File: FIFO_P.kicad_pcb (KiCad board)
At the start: 4 copper layers, 100 x 100 mm, 76 parts, among them J1 Vin +, J2 Vin -, J3 ICLK, J4 Vout, J5 Jack-DC, SW1 Rotary_Encoder_61C, U1 SN74LVC2G157_MUX_TI, U10 AD7840, U11 LM2940CT-5.0, U12 UA79M05CKCS_-5V, U13 LM2940CT-3.3, U2 IDT_ICS551, U3 LTC1740, U4 ARDUINO_DUE_FIFO_P_COMMANDS, U5 IDT_72V2105, U6 TXB0104, U7 TXB0104, U8 TXB0104, U9 TXB0104

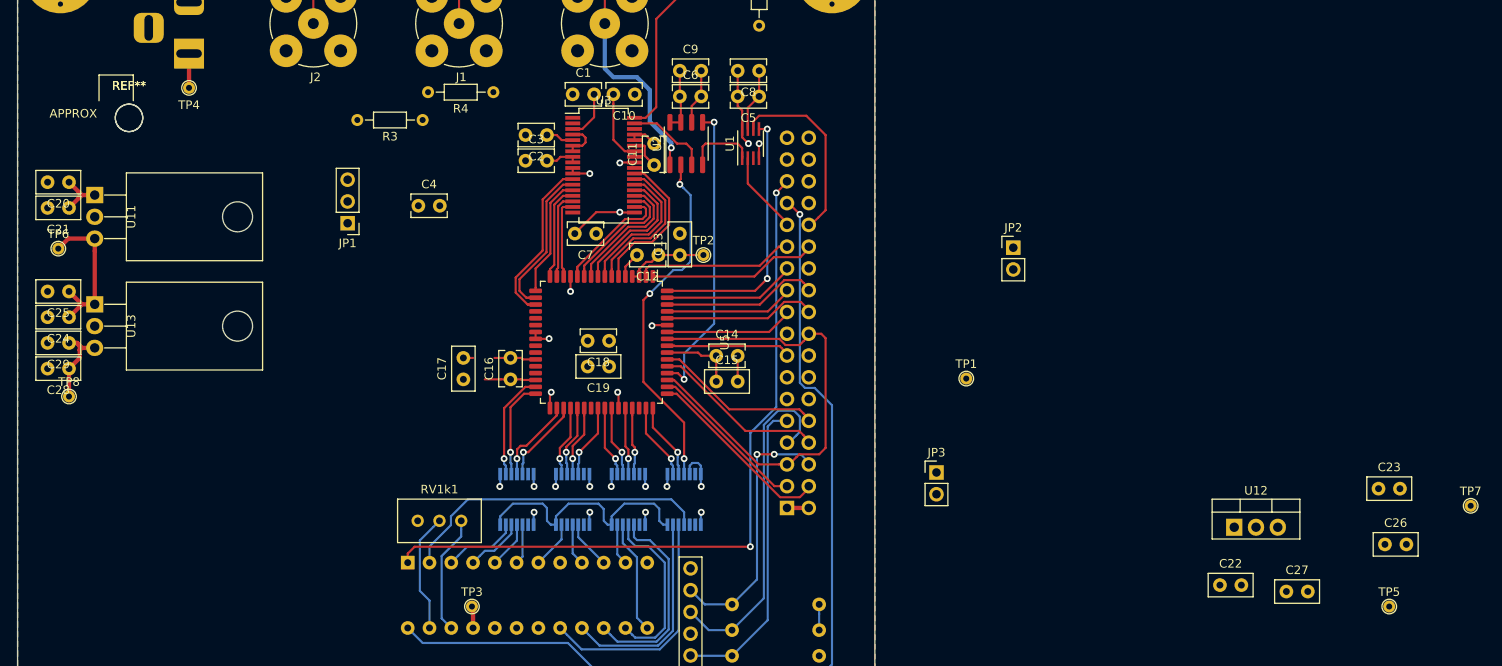
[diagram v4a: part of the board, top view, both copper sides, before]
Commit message: Added inverter for -5V
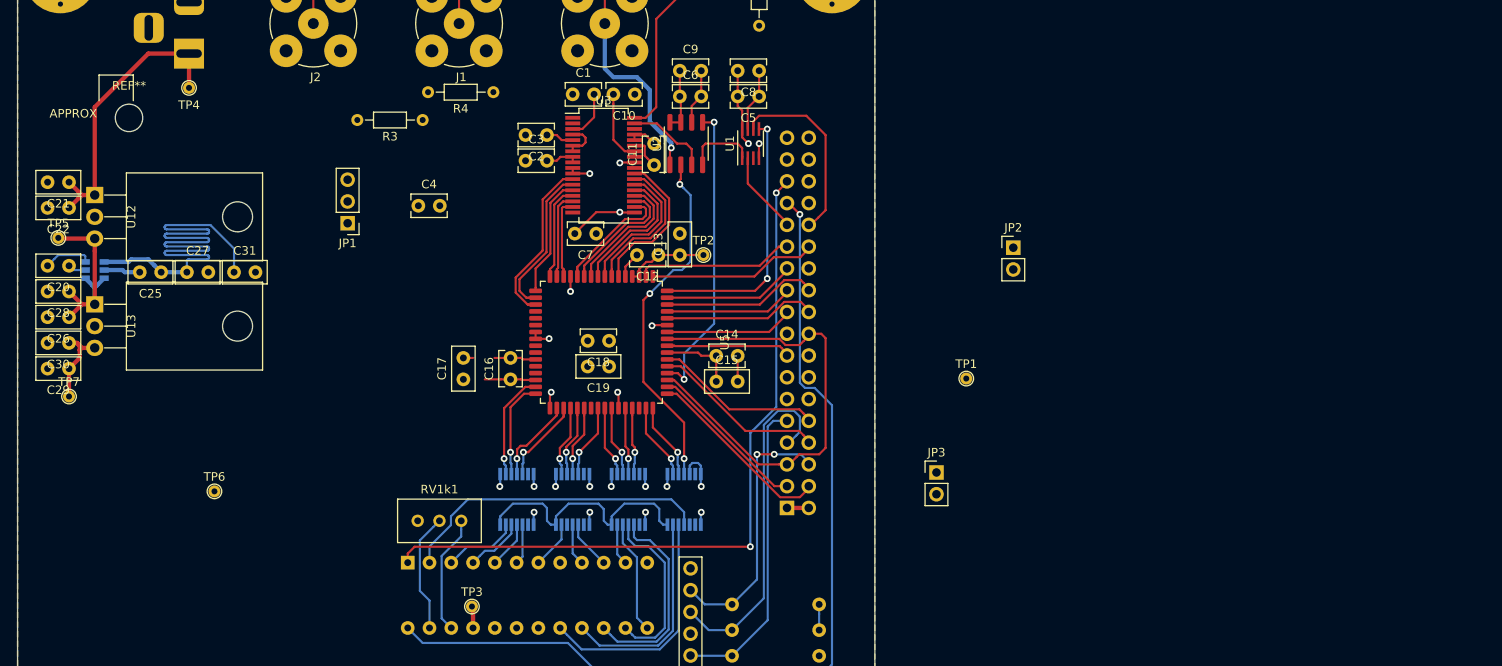
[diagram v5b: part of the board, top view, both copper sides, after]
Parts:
- removed the C22 at (189.8, 125.5)
- removed C23: .47uF, Capacitor_THT:C_Disc_D5.0mm_W2.5mm_P2.50mm
- removed the C26 at (209.0, 120.8)
- removed the REF** at (62.5, 71.0)
- removed the TP5 at (209.5, 128.0)
- removed the TP7 at (219.0, 116.2)
- removed the U12 at (191.4, 118.8)
- added C20: .47uF, Capacitor_THT:C_Disc_D5.0mm_W2.5mm_P2.50mm, F.Cu at (55.5, 88.2)
- added C25: .47uF, Capacitor_THT:C_Disc_D5.0mm_W2.5mm_P2.50mm, F.Cu at (66.2, 89.0)
- added C31: 22uF, Capacitor_THT:C_Disc_D5.0mm_W2.5mm_P2.50mm, F.Cu at (74.8, 89.0)
- added TP6: TestPoint, FIFO_P:Test_Pin, F.Cu at (72.5, 114.6)
- added U11: LM2776, Package_TO_SOT_SMD:SOT-23-6, B.Cu at (58.5, 88.8)
- C27: value .47uF -> 22uF
- moved C27 133.6 mm to (69.2, 89.0)
- moved TP5 1.25 mm to (54.2, 85.0)
- renumbered C20 to C21, C21 to C22, C24 to C26, C25 to C28, C28 to C29, C29 to C30, TP6 to TP5, TP8 to TP7, U11 to U12
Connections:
- C12 pad 2: GND -> +5V
- C13 pad 2: GND -> +5V
- C14 pad 2: GND -> +5V
- C15 pad 2: GND -> +5V
- C16 pad 2: GND -> +5V
- C17 pad 2: GND -> +5V
- C18 pad 1: GND -> +5V
- C19 pad 1: GND -> +5V
- C21 pad 2: GND -> +5V
- C22 pad 2: GND -> +5V
- C26 pad 2: GND -> +5V
- C27 pad 2: Net-(C22-Pad2) -> +5V
- C28 pad 2: GND -> +5V
- C29 pad 2: GND -> +5V
- C30 pad 2: GND -> +5V
- C5 pad 1: GND -> +5V
- C6 pad 2: GND -> +5V
- C7 pad 1: GND -> +5V
- C8 pad 1: GND -> +5V
- C9 pad 2: GND -> +5V
- J3 pad 2: GND -> +5V
- J5 pad 2: GND -> +5V
- JP2 pad 1: GND -> +5V
- JP3 pad 1: GND -> +5V
- R5 pad 2: GND -> +5V
- R6 pad 2: GND -> +5V
- R8 pad 1: GND -> +5V
- RV1k1 pad 3: GND -> +5V
- SW1 pad 1: GND -> +5V
- U1 pad 4: GND -> +5V
- U1 pad 7: GND -> +5V
- U10 pad 12: GND -> +5V
- U12 pad 2: GND -> +5V
- U13 pad 2: GND -> +5V
- U2 pad 6: GND -> +5V
- U3 pad 10: GND -> +5V
- U3 pad 11: GND -> +5V
- U3 pad 28: GND -> +5V
- U4 pad GND: GND -> +5V
- U5 pad 13: GND -> +5V
- U5 pad 23: GND -> +5V
- U5 pad 24: GND -> +5V
- U5 pad 27: GND -> +5V
- U5 pad 33: GND -> +5V
- U5 pad 39: GND -> +5V
- U5 pad 46: GND -> +5V
- U5 pad 5: GND -> +5V
- U5 pad 59: GND -> +5V
- U6 pad 7: GND -> +5V
- U7 pad 7: GND -> +5V
- U8 pad 7: GND -> +5V
- U9 pad 5: GND -> +5V
- U9 pad 7: GND -> +5V
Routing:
- net -5V: track 11.5 -> 76.4 mm
- net +5V: track 58.5 -> 117.3 mm, vias 0 -> 11
- net GND: track 49.5 -> 0.00 mm, vias 11 -> 0
- net Net-(C21-Pad1): track 10.5 -> 34.3 mm
- net Net-(C20-Pad2): track 0.00 -> 5.64 mm
- net Net-(C20-Pad1): track 0.00 -> 2.11 mm
- added copper zone on B.Cu, net +5V
- added copper zone on In1.Cu, net +5V
- removed copper zone on B.Cu, net -5V
- removed copper zone on In1.Cu, net GND

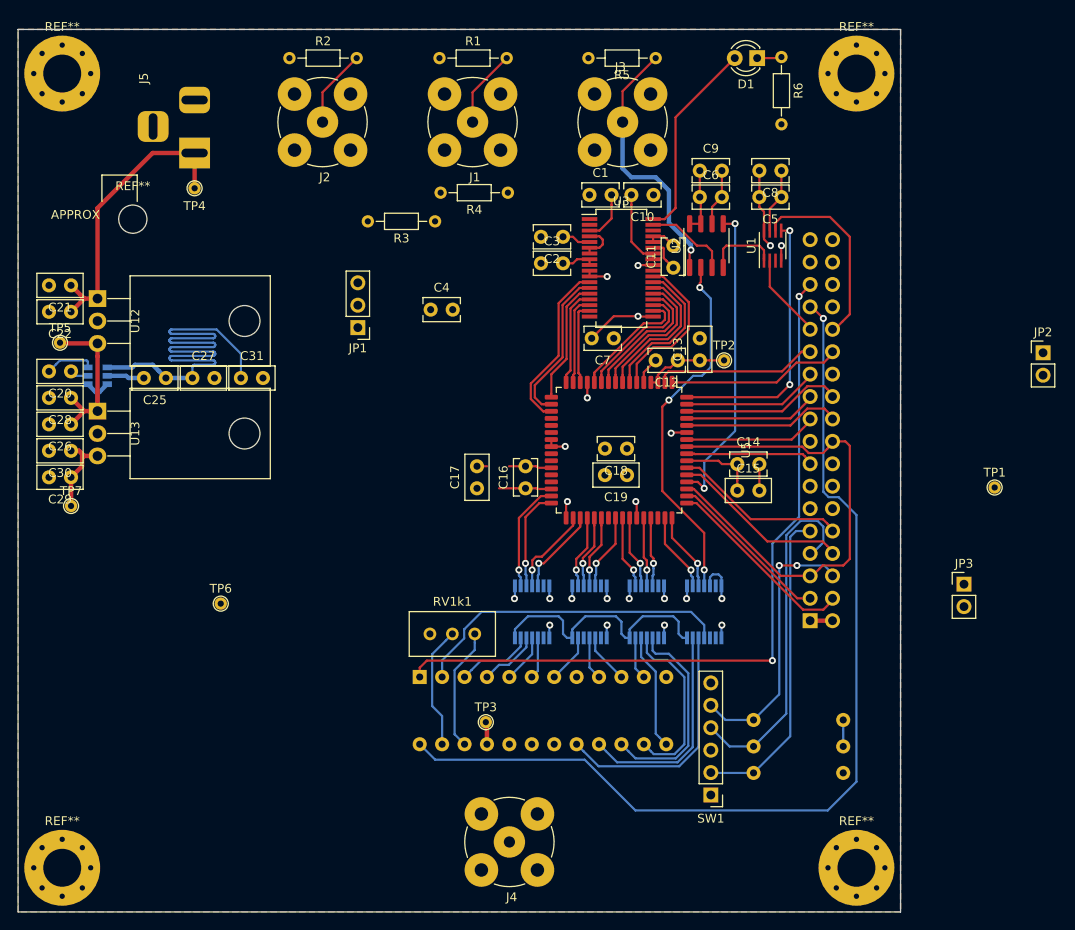
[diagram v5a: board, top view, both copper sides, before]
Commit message: Partial jumpers
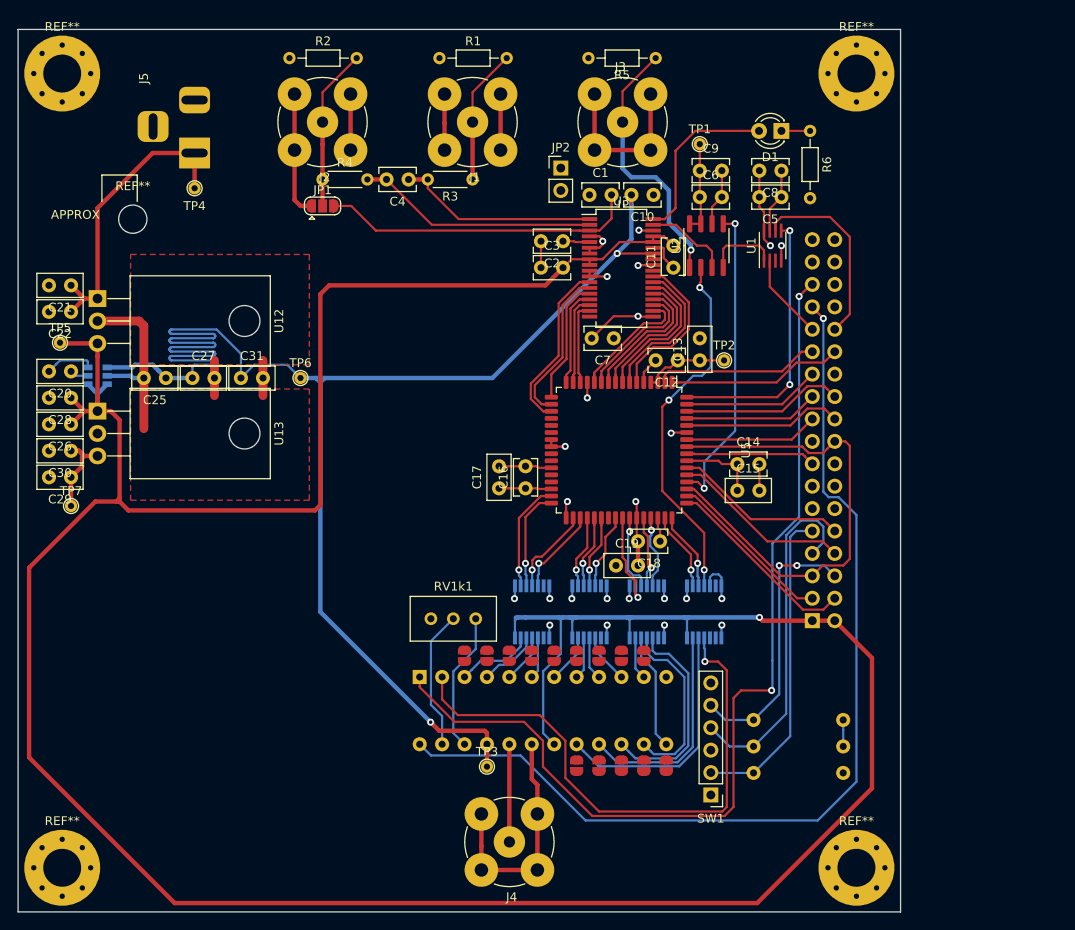
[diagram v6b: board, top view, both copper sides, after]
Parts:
- removed JP3: Jumper, Connector_PinHeader_2.54mm:PinHeader_1x02_P2.54mm_Vertical
- added REF**: SolderJumper-2_P1.3mm_Open_RoundedPad1.0x1.5mm, Jumper:SolderJumper-2_P1.3mm_Open_RoundedPad1.0x1.5mm, F.Cu at (112.8, 132.9)
- added REF**: SolderJumper-2_P1.3mm_Open_RoundedPad1.0x1.5mm, Jumper:SolderJumper-2_P1.3mm_Open_RoundedPad1.0x1.5mm, F.Cu at (110.2, 120.5)
- added REF**: SolderJumper-2_P1.3mm_Open_RoundedPad1.0x1.5mm, Jumper:SolderJumper-2_P1.3mm_Open_RoundedPad1.0x1.5mm, F.Cu at (107.7, 120.5)
- added REF**: SolderJumper-2_P1.3mm_Open_RoundedPad1.0x1.5mm, Jumper:SolderJumper-2_P1.3mm_Open_RoundedPad1.0x1.5mm, F.Cu at (105.2, 120.5)
- added REF**: SolderJumper-2_P1.3mm_Open_RoundedPad1.0x1.5mm, Jumper:SolderJumper-2_P1.3mm_Open_RoundedPad1.0x1.5mm, F.Cu at (102.6, 120.5)
- added REF**: SolderJumper-2_P1.3mm_Open_RoundedPad1.0x1.5mm, Jumper:SolderJumper-2_P1.3mm_Open_RoundedPad1.0x1.5mm, F.Cu at (100.1, 120.5)
- added REF**: SolderJumper-2_P1.3mm_Open_RoundedPad1.0x1.5mm, Jumper:SolderJumper-2_P1.3mm_Open_RoundedPad1.0x1.5mm, F.Cu at (115.3, 132.9)
- added REF**: SolderJumper-2_P1.3mm_Open_RoundedPad1.0x1.5mm, Jumper:SolderJumper-2_P1.3mm_Open_RoundedPad1.0x1.5mm, F.Cu at (117.9, 132.9)
- added REF**: SolderJumper-2_P1.3mm_Open_RoundedPad1.0x1.5mm, Jumper:SolderJumper-2_P1.3mm_Open_RoundedPad1.0x1.5mm, F.Cu at (120.4, 132.9)
- added REF**: SolderJumper-2_P1.3mm_Open_RoundedPad1.0x1.5mm, Jumper:SolderJumper-2_P1.3mm_Open_RoundedPad1.0x1.5mm, F.Cu at (123.0, 132.9)
- added REF**: SolderJumper-2_P1.3mm_Open_RoundedPad1.0x1.5mm, Jumper:SolderJumper-2_P1.3mm_Open_RoundedPad1.0x1.5mm, F.Cu at (120.4, 120.5)
- added REF**: SolderJumper-2_P1.3mm_Open_RoundedPad1.0x1.5mm, Jumper:SolderJumper-2_P1.3mm_Open_RoundedPad1.0x1.5mm, F.Cu at (117.9, 120.5)
- added REF**: SolderJumper-2_P1.3mm_Open_RoundedPad1.0x1.5mm, Jumper:SolderJumper-2_P1.3mm_Open_RoundedPad1.0x1.5mm, F.Cu at (115.3, 120.5)
- added REF**: SolderJumper-2_P1.3mm_Open_RoundedPad1.0x1.5mm, Jumper:SolderJumper-2_P1.3mm_Open_RoundedPad1.0x1.5mm, F.Cu at (112.8, 120.5)
- JP1: footprint Connector_PinHeader_2.54mm:PinHeader_1x03_P2.54mm_Vertical -> Jumper:SolderJumper-3_P1.3mm_Open_RoundedPad1.0x1.5mm
- R3, R4: footprint Resistor_THT:R_Axial_DIN0204_L3.6mm_D1.6mm_P7.62mm_Horizontal -> Resistor_THT:R_Axial_DIN0204_L3.6mm_D1.6mm_P5.08mm_Horizontal
- moved JP2 58.5 mm to (111.0, 65.2)
- moved TP1 51.3 mm to (126.8, 62.5)
- moved TP6 27.1 mm to (81.5, 89.0)
- moved R4 21.1 mm to (84.0, 66.5), turned to 0 degrees
- moved C4 15.0 mm to (93.8, 66.5), turned to 180 degrees
- moved JP1 14.4 mm to (84.0, 69.5), turned to 0 degrees
- moved C18 11.1 mm to (122.2, 107.5)
- moved C19 10.3 mm to (117.2, 110.2), turned to 0 degrees
- moved R6 8.98 mm to (139.2, 61.0)
- moved D1 8.70 mm to (136.0, 61.0)
- moved R3 6.37 mm to (101.0, 66.5)
- moved TP3 5.04 mm to (102.6, 133.0)
- moved C17 2.50 mm to (104.0, 101.5)
- moved RV1k1 1.73 mm to (101.4, 116.3)
- moved C2 0.50 mm to (111.2, 73.5)
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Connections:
- C12 pad 2: +5V -> GND
- C13 pad 2: +5V -> GND
- C14 pad 2: +5V -> GND
- C15 pad 2: +5V -> GND
- C16 pad 2: +5V -> GND
- C17 pad 2: +5V -> GND
- C18 pad 1: +5V -> GND
- C19 pad 1: +5V -> GND
- C21 pad 2: +5V -> GND
- C22 pad 2: +5V -> GND
- C25 pad 2: +5V -> GND
- C26 pad 2: +5V -> GND
- C27 pad 2: +5V -> GND
- C28 pad 2: +5V -> GND
- C29 pad 2: +5V -> GND
- C30 pad 2: +5V -> GND
- C31 pad 2: +5V -> GND
- C5 pad 1: +5V -> GND
- C6 pad 2: +5V -> GND
- C7 pad 1: +5V -> GND
- C8 pad 1: +5V -> GND
- C9 pad 2: +5V -> GND
- J3 pad 2: +5V -> GND
- J5 pad 2: +5V -> GND
- JP2 pad 1: +5V -> GND
- R5 pad 2: +5V -> GND
- R6 pad 2: +5V -> GND
- R8 pad 1: +5V -> GND
- RV1k1 pad 3: +5V -> GND
- SW1 pad 1: +5V -> GND
- U1 pad 4: +5V -> GND
- U1 pad 7: +5V -> GND
- U10 pad 12: +5V -> GND
- U11 pad 2: +5V -> GND
- U12 pad 2: +5V -> GND
- U13 pad 2: +5V -> GND
- U2 pad 6: +5V -> GND
- U3 pad 10: +5V -> GND
- U3 pad 11: +5V -> GND
- U3 pad 28: +5V -> GND
- U4 pad GND: +5V -> GND
- U5 pad 13: +5V -> GND
- U5 pad 23: +5V -> GND
- U5 pad 24: +5V -> GND
- U5 pad 27: +5V -> GND
- U5 pad 33: +5V -> GND
- U5 pad 39: +5V -> GND
- U5 pad 46: +5V -> GND
- U5 pad 5: +5V -> GND
- U5 pad 59: +5V -> GND
- U6 pad 7: +5V -> GND
- U7 pad 7: +5V -> GND
- U8 pad 7: +5V -> GND
- U9 pad 5: +5V -> GND
- U9 pad 7: +5V -> GND
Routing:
- net +5V: track 117.3 -> 356.2 mm, vias 11 -> 1
- net -5V: track 76.4 -> 183.6 mm, vias 0 -> 2
- net GND: track 0.00 -> 100.7 mm, vias 0 -> 11
- net GNDA: track 8.37 -> 46.2 mm, vias 0 -> 2
- net Net-(C1-Pad2): track 5.73 -> 35.8 mm
- net Net-(C4-Pad2): track 0.00 -> 27.3 mm
- net LDAC5V: track 36.5 -> 63.8 mm, vias 0 -> 1
- net Net-(J4-Pad2): track 0.00 -> 27.2 mm
- net Net-(U10-Pad1): track 85.9 -> 109.9 mm
- net Net-(C4-Pad1): track 0.00 -> 22.9 mm
- net Net-(J4-Pad1): track 0.00 -> 11.1 mm
- net Net-(J2-Pad1): track 8.85 -> 18.4 mm
- net 3.3V: track 76.8 -> 85.2 mm
- net Net-(J1-Pad1): track 8.85 -> 15.4 mm
- net Net-(U10-Pad8): track 0.71 -> 5.47 mm
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- added copper zone on F.Cu, net GND
- added copper zone on In1.Cu, net GND
- added copper zone on In1.Cu, net GNDA
- removed copper zone on B.Cu, net +5V
- removed copper zone on F.Cu, net +5V
- removed copper zone on In1.Cu, net +5V

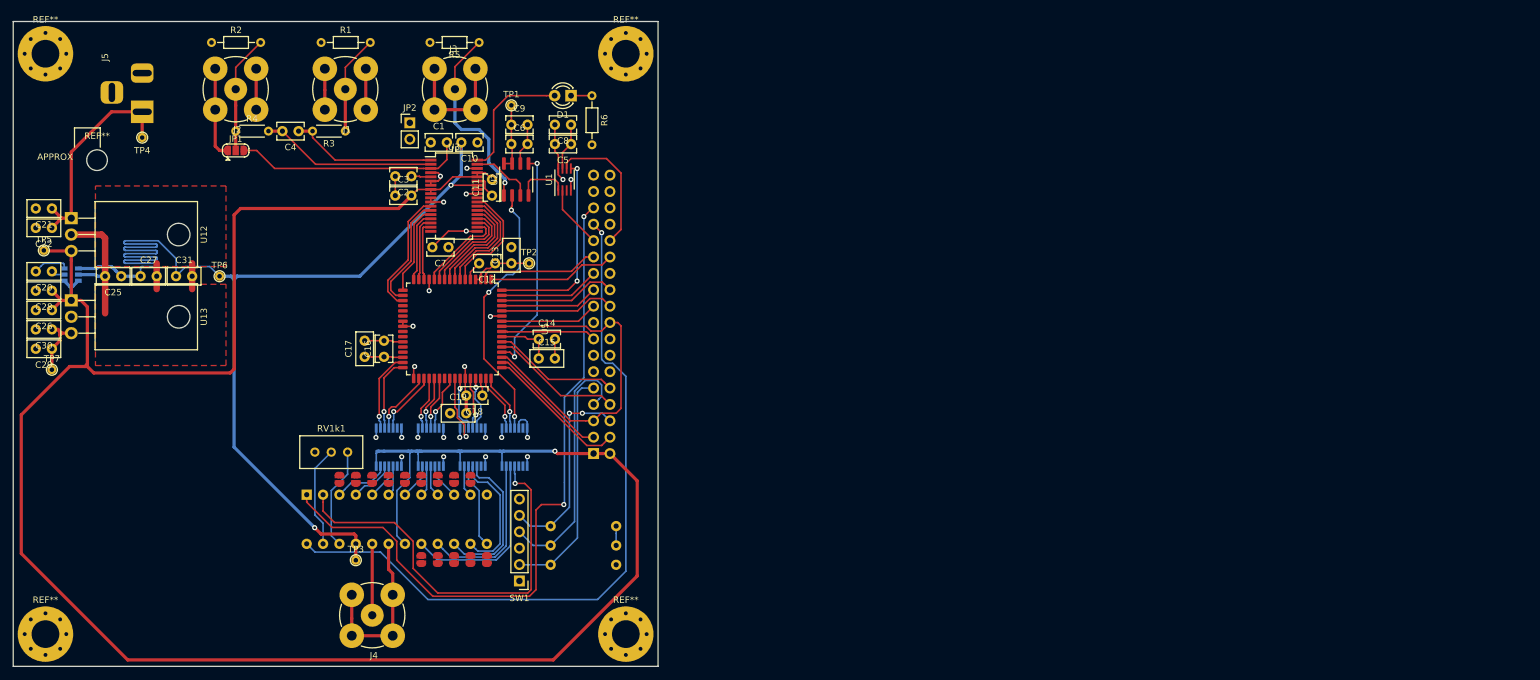
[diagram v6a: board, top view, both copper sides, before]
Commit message: Cleanup; prepared to route header
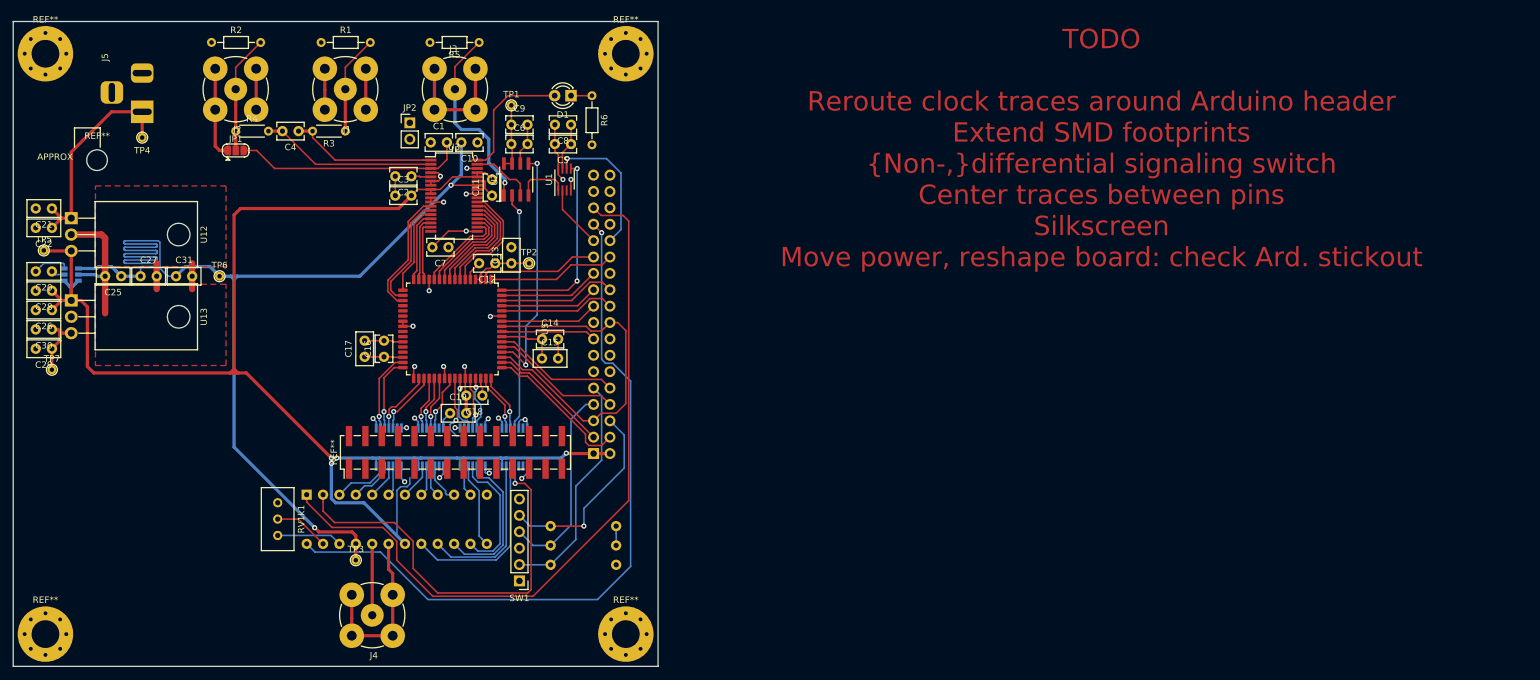
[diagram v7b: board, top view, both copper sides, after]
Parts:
- removed the REF** at (112.8, 132.9)
- removed the REF** at (110.2, 120.5)
- removed the REF** at (107.7, 120.5)
- removed the REF** at (105.2, 120.5)
- removed the REF** at (102.6, 120.5)
- removed the REF** at (100.1, 120.5)
- removed the REF** at (115.3, 132.9)
- removed the REF** at (117.9, 132.9)
- removed the REF** at (120.4, 132.9)
- removed the REF** at (123.0, 132.9)
- removed the REF** at (120.4, 120.5)
- removed the REF** at (117.9, 120.5)
- removed the REF** at (115.3, 120.5)
- removed the REF** at (112.8, 120.5)
- added REF**: PinHeader_2x14_P2.54mm_Vertical_SMD, Connector_PinHeader_2.54mm:PinHeader_2x14_P2.54mm_Vertical_SMD, F.Cu at (118.1, 116.3)
- moved RV1k1 16.9 mm to (90.5, 129.2), turned to 270 degrees
- moved C14 0.50 mm to (131.5, 98.8)
- moved C15 0.50 mm to (131.5, 101.8)
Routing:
- net +5V: track 356.2 -> 235.5 mm, vias 1 -> 4
- net Net-(R7-Pad2): track 39.9 -> 31.1 mm
- net Net-(RV1k1-Pad2): track 15.8 -> 8.62 mm
- net Net-(RV1k1-Pad1): track 15.8 -> 10.1 mm
- net Net-(U10-Pad1): track 109.9 -> 114.8 mm, vias 2 -> 0
- net LDAC: track 41.5 -> 36.9 mm, vias 3 -> 1
- net 3.3V: track 85.2 -> 89.0 mm
- net RCLK: track 35.1 -> 37.9 mm
- net GND: track 100.7 -> 101.9 mm
- net Net-(U5-Pad41): track 11.2 -> 12.4 mm
- net Net-(U4-Pad23): track 22.3 -> 23.0 mm
- net Net-(U10-Pad10): track 5.66 -> 6.32 mm
- net Net-(U4-Pad24): track 56.3 -> 56.9 mm
- net Net-(U10-Pad24): track 111.4 -> 112.0 mm
- net Net-(R9-Pad2): track 31.0 -> 30.5 mm, vias 2 -> 1
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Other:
- board text added: "TODO Reroute clock traces around Arduino header Extend SMD footprints {Non-,}differential signaling switch Center traces between pins Silkscreen Move power, reshape board: check Ard. stickout"
